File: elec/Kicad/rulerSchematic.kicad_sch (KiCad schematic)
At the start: 0 parts

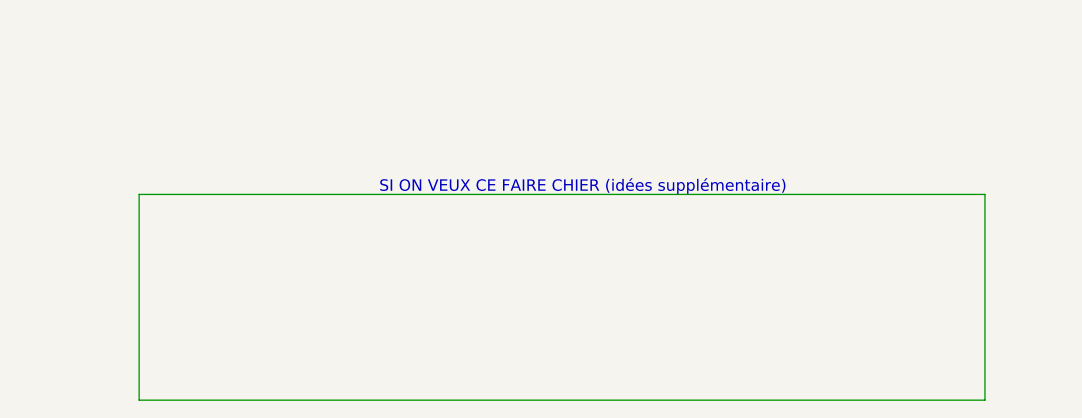
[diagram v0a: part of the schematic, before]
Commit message: add the MCU and embedded deboger footprint in the schematic
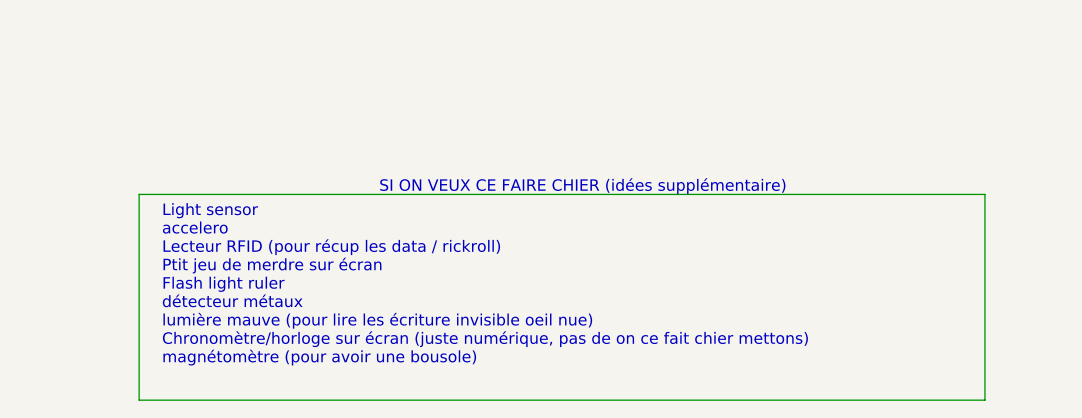
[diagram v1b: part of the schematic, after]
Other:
- note added: "Light sensor accelero Lecteur RFID (pour récup les data / rickroll) Ptit jeu de merdre sur écran Flash light ruler détecteur métaux lumière mauve (pour lire les écriture invisible oeil nue) Chronomètre/horloge sur écran (juste numérique, pas de on ce fait chier mettons) magnétomètre (pour avoir une bousole)"
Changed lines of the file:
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@@
     (stroke (width 0) (type default) (color 0 0 0 0))
+  )
+  (text "Light sensor\naccelero\nLecteur RFID (pour récup les data / rickroll)\nPtit jeu de merdre sur écran\nFlash light ruler\ndétecteur métaux\nlumière mauve (pour lire les écriture invisible oeil nue)\nChronomètre/horloge sur écran (juste numérique, pas de on ce fait chier mettons)\nmagnétomètre (pour avoir une bousole)"
+    (at 182.88 152.4 0)
+    (effects (font (size 1.27 1.27)) (justify left bottom))
   )
   (text "SI ON VEUX CE FAIRE CHIER (idées supplémentaire)" (at 207.01 133.35 0)
@@
     (path "/60d26db4-b138-46b0-b681-4276ebd1d4cf" (page "7"))
     (path "/494e6d32-1eab-4497-b57f-12dbcea47915" (page "8"))
+    (path "/47f0fc71-ff78-496f-bb04-036a9aeaa71c/67140130-f424-4e39-9322-f3f2812be349" (page "9"))
+  )
+  (symbol_instances
+    (path "/47f0fc71-ff78-496f-bb04-036a9aeaa71c/d4d5e971-027b-4246-b05f-a0a5aaaf53df"
+      (reference "U1") (unit 1) (value "STM32L053C8T6") (footprint "Package_QFP:LQFP-48_7x7mm_P0.5mm")
+    )
+    (path "/47f0fc71-ff78-496f-bb04-036a9aeaa71c/67140130-f424-4e39-9322-f3f2812be349/38637a6f-6799-45d7-a122-bdd57b2f9701"
+      (reference "U2") (unit 1) (value "STM32F103CBT6") (footprint "Package_QFP:LQFP-48_7x7mm_P0.5mm")
+    )
   )
 )

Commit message: formation torture
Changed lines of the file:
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@@
 	(generator_version "8.0")
 	(paper "A4")
-	(wire
-		(pts
-			(xy 274.32 133.35) (xy 180.34 133.35)
-		)
+	(rectangle
+		(start 181.61 133.35)
+		(end 267.97 154.94)
 		(stroke
 			(width 0)
-			(type default)
+			(type dash)
+		)
+		(fill
+			(type none)
 		)
 	)
-	(wire
-		(pts
-			(xy 180.34 156.21) (xy 274.32 156.21)
-		)
-		(stroke
-			(width 0)
-			(type default)
-		)
-	)
-	(wire
-		(pts
-			(xy 180.34 133.35) (xy 180.34 156.21)
-		)
-		(stroke
-			(width 0)
-			(type default)
-		)
-	)
-	(wire
-		(pts
-			(xy 274.32 156.21) (xy 274.32 133.35)
-		)
-		(stroke
-			(width 0)
-			(type default)
-		)
-	)

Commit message: généré la schematic
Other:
- note removed: "Light sensor accelero Lecteur RFID (pour récup les data / rickroll) Ptit jeu de merdre sur écran Flash light ruler détecteur métaux lumière mauve (pour lire les écriture invisible oeil nue) Chronomètre/horloge sur écran (juste numérique, pas de on ce fait chier mettons) magnétomètre (pour avoir une bousole)"
- note removed: "SI ON VEUX CE FAIRE CHIER (idées supplémentaire)"
- company: (none) -> University of Sherbrooke
- title: (none) -> Touillometre - Root 
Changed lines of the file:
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@@
 	(generator_version "8.0")
 	(paper "A4")
-	(rectangle
-		(start 181.61 133.35)
-		(end 267.97 154.94)
-		(stroke
-			(width 0)
-			(type dash)
-		)
-		(fill
-			(type none)
-		)
-	)
-	(text "Light sensor\naccelero\nLecteur RFID (pour récup les data / rickroll)\nPtit jeu de merdre sur écran\nFlash light ruler\ndétecteur métaux\nlumière mauve (pour lire les écriture invisible oeil nue)\nChronomètre/horloge sur écran (juste numérique, pas de on ce fait chier mettons)\nmagnétomètre (pour avoir une bousole)"
-		(exclude_from_sim no)
-		(at 182.88 152.4 0)
-		(effects
-			(font
-				(size 1.27 1.27)
-			)
-			(justify left bottom)
-		)
-	)
-	(text "SI ON VEUX CE FAIRE CHIER (idées supplémentaire)"
-		(exclude_from_sim no)
-		(at 207.01 133.35 0)
-		(effects
-			(font
-				(size 1.27 1.27)
-			)
-			(justify left bottom)
-		)
+	(title_block
+		(title "Touillometre - Root ")
+		(date "2024-12-26")
+		(rev "C3I")
+		(company "University of Sherbrooke")
 	)
 	(sheet
